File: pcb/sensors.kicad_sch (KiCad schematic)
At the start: 6 parts, among them U3 INA230AIRGTT, U4 MCP9804_DFN, U6 INA230AIRGTT, U7 INA230AIRGTT

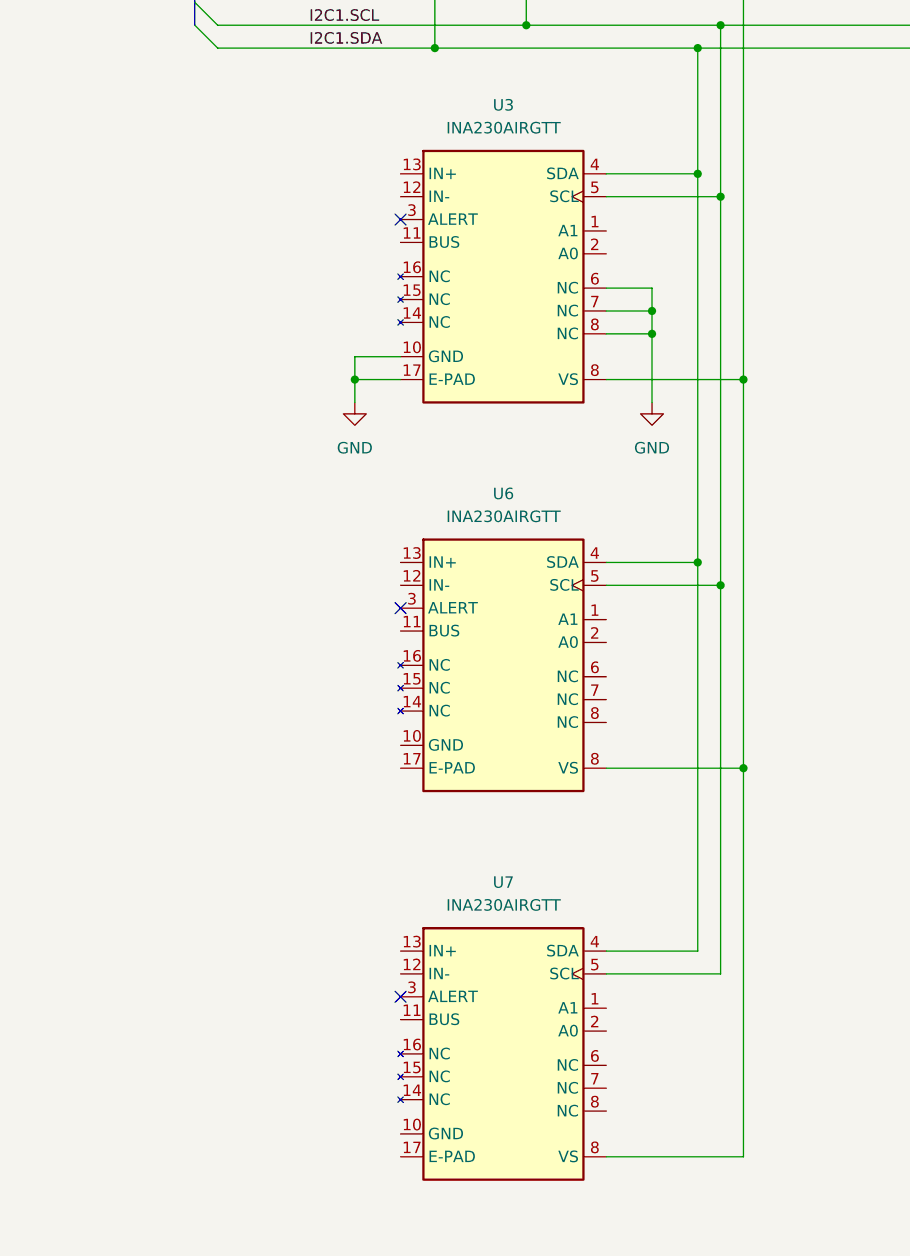
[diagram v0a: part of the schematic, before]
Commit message: hierarchical current sense
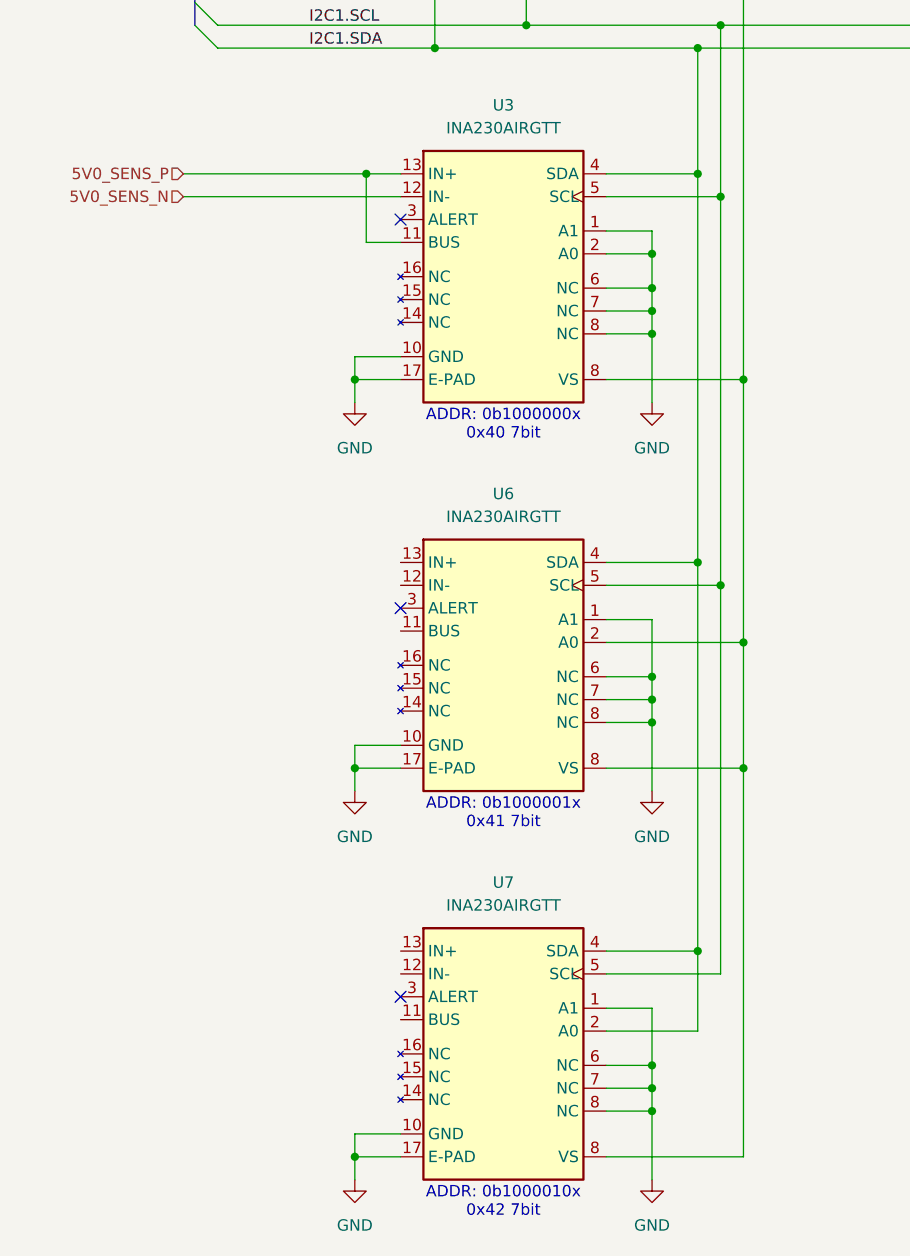
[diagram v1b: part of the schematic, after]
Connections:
- net 3V3: now also U6.2 (A0)
- net GND: now also U3.1 (A1), U3.2 (A0), U6.1 (A1), U6.10 (GND), U6.17 (E-PAD), U6.6 (NC), U6.7 (NC), U6.8 (VS), U7.1 (A1), U7.10 (GND), U7.17 (E-PAD), U7.6 (NC), U7.7 (NC), U7.8 (VS)
- net I2C1.SDA: now also U7.2 (A0)
- net 5V0_SENS_P: now reaches U3.11 (BUS)
- net 5V0_SENS_P: now also U3.13 (IN+)
- net 5V0_SENS_N: now reaches U3.12 (IN-)
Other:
- note added: "ADDR: 0b1000000x 0x40 7bit"
- note added: "ADDR: 0b1000001x 0x41 7bit"
- note added: "ADDR: 0b1000010x 0x42 7bit"

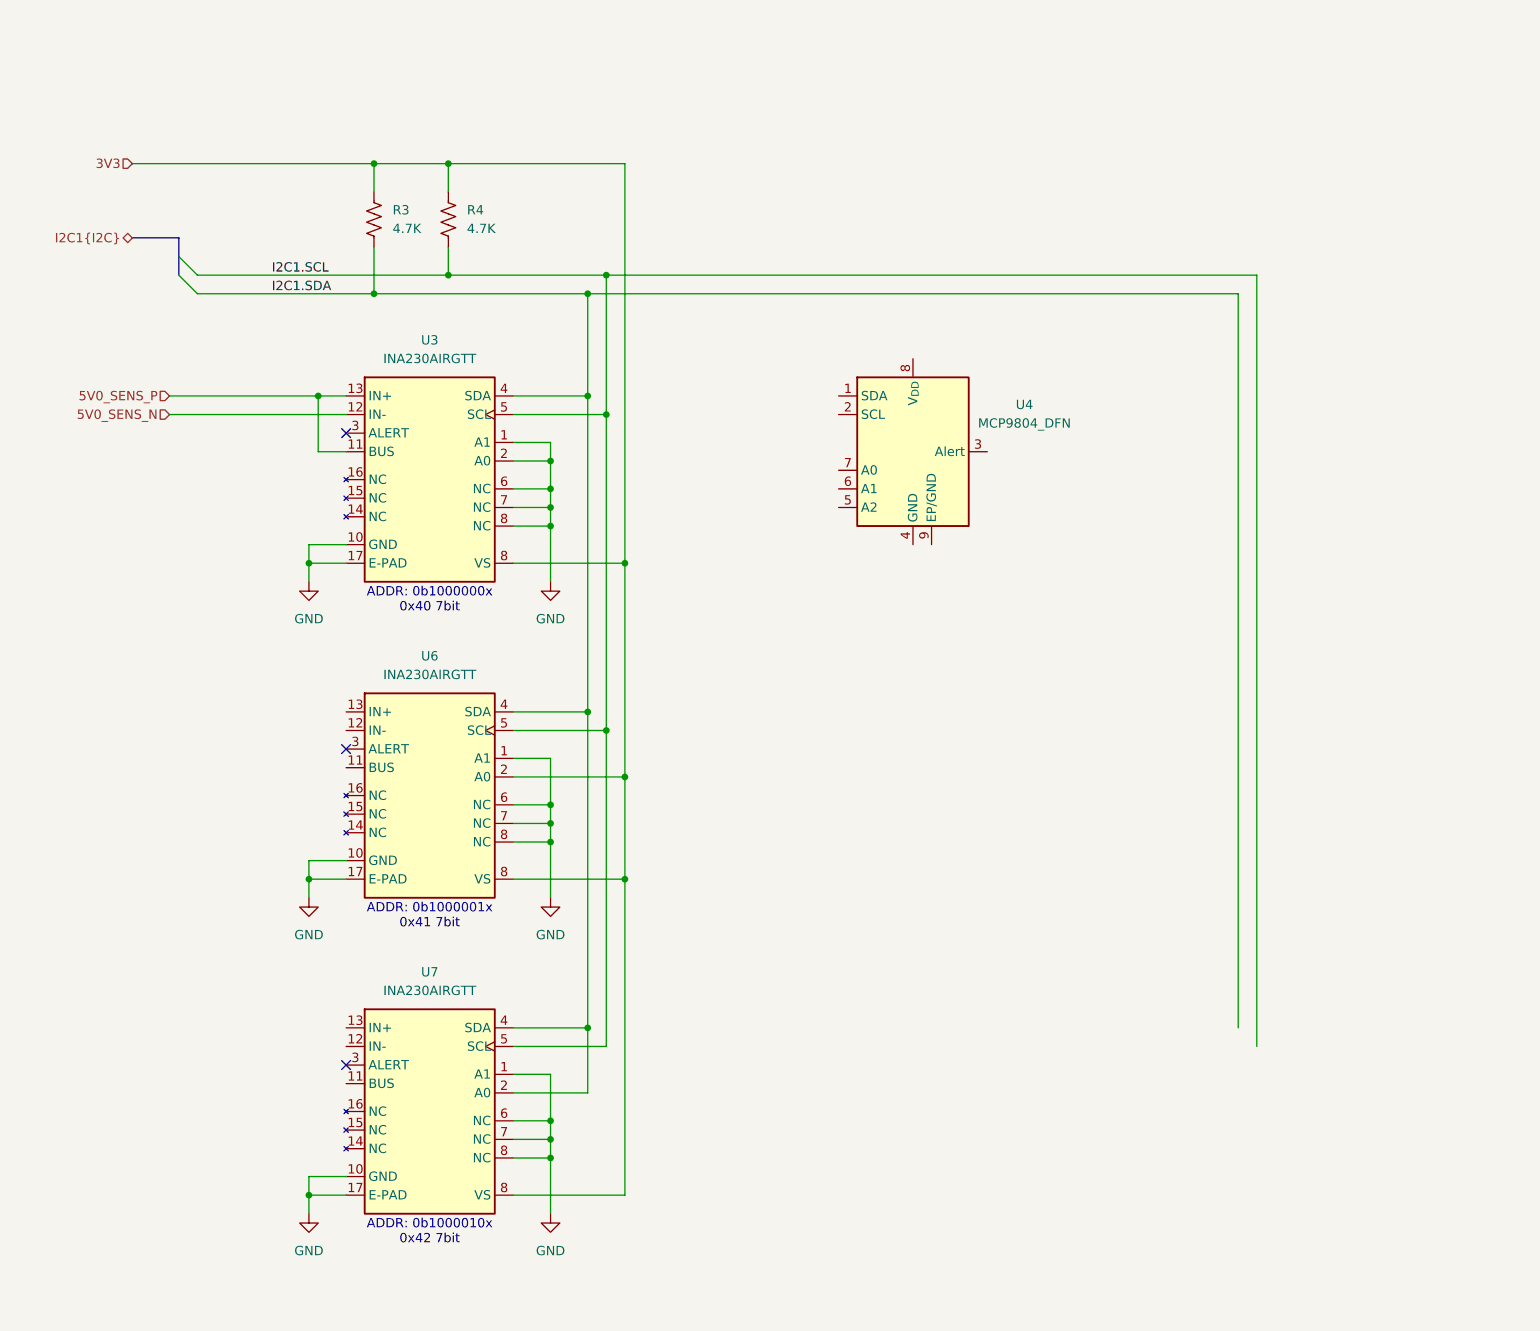
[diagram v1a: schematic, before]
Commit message: current sense hierarchy definition
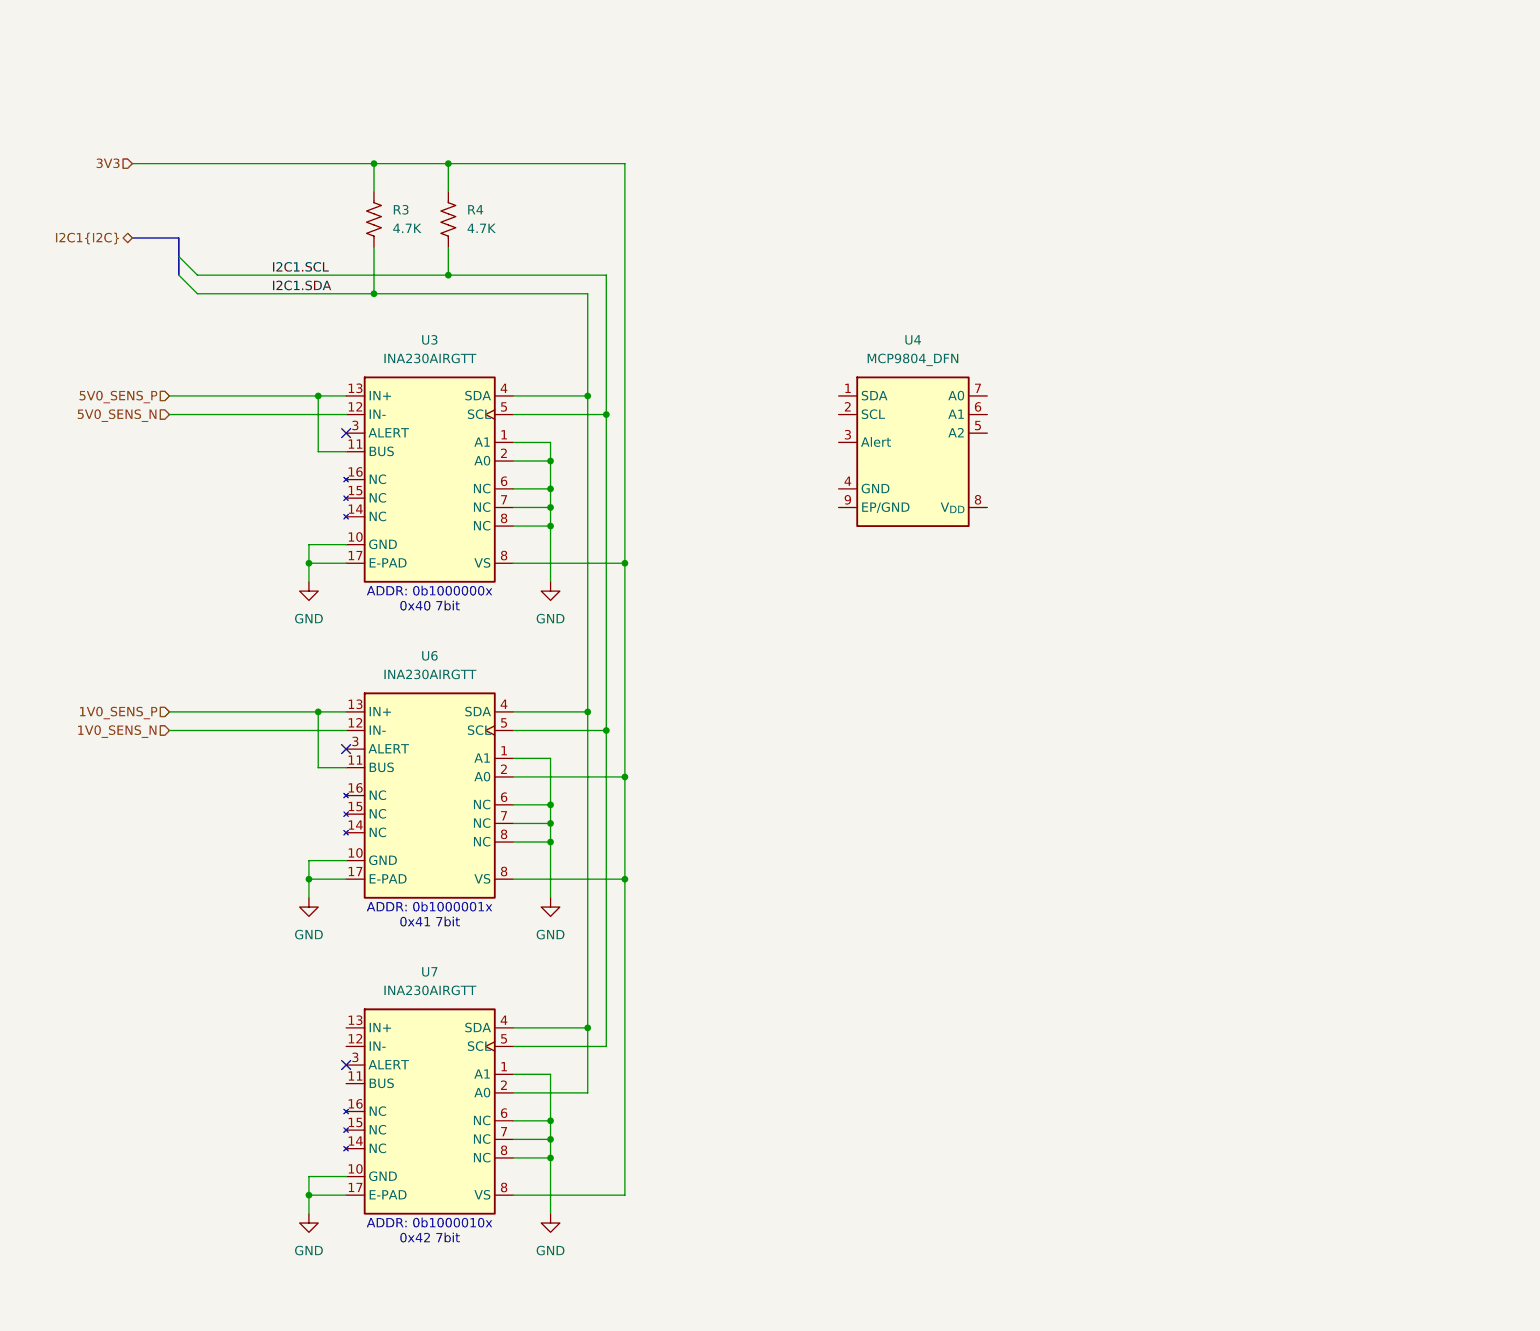
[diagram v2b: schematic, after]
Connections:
- net 1V0_SENS_P: now reaches U6.11 (BUS)
- net 1V0_SENS_P: now also U6.13 (IN+)
- net 1V0_SENS_N: now reaches U6.12 (IN-)
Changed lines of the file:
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@@
-	)
-	(junction
-		(at 104.14 54.61)
-		(diameter 0)
-		(color 0 0 0 0)
 	)
 	(junction
@@
 	)
 	(junction
+		(at 67.31 111.76)
+		(diameter 0)
+		(color 0 0 0 0)
+	)
+	(junction
 		(at 85.09 36.83)
 		(diameter 0)
@@
 	(junction
 		(at 106.68 71.12)
-		(diameter 0)
-		(color 0 0 0 0)
-	)
-	(junction
-		(at 106.68 52.07)
 		(diameter 0)
 		(color 0 0 0 0)
@@
 	(wire
 		(pts
+			(xy 46.99 114.3) (xy 71.12 114.3)
+		)
+		(stroke
+			(width 0)
+			(type default)
+		)
+	)
+	(wire
+		(pts
 			(xy 99.06 118.11) (xy 99.06 124.46)
 		)
@@
 	(wire
 		(pts
-			(xy 193.04 54.61) (xy 193.04 154.94)
-		)
-		(stroke
-			(width 0)
-			(type default)
-		)
-	)
-	(wire
-		(pts
 			(xy 104.14 154.94) (xy 104.14 111.76)
 		)
@@
 	(wire
 		(pts
+			(xy 46.99 111.76) (xy 67.31 111.76)
+		)
+		(stroke
+			(width 0)
+			(type default)
+		)
+	)
+	(wire
+		(pts
 			(xy 99.06 170.18) (xy 99.06 172.72)
 		)
@@
 	(wire
 		(pts
-			(xy 195.58 52.07) (xy 195.58 157.48)
-		)
-		(stroke
-			(width 0)
-			(type default)
-		)
-	)
-	(wire
-		(pts
 			(xy 109.22 91.44) (xy 93.98 91.44)
 		)
@@
 	(wire
 		(pts
-			(xy 195.58 52.07) (xy 106.68 52.07)
-		)
-		(stroke
-			(width 0)
-			(type default)
-		)
-	)
-	(wire
-		(pts
 			(xy 99.06 124.46) (xy 99.06 127)
 		)
@@
 	(wire
 		(pts
+			(xy 67.31 119.38) (xy 67.31 111.76)
+		)
+		(stroke
+			(width 0)
+			(type default)
+		)
+	)
+	(wire
+		(pts
 			(xy 93.98 127) (xy 99.06 127)
 		)
@@
 	(wire
 		(pts
+			(xy 67.31 111.76) (xy 71.12 111.76)
+		)
+		(stroke
+			(width 0)
+			(type default)
+		)
+	)
+	(wire
+		(pts
 			(xy 93.98 118.11) (xy 99.06 118.11)
 		)
@@
 	(wire
 		(pts
-			(xy 193.04 54.61) (xy 104.14 54.61)
-		)
-		(stroke
-			(width 0)
-			(type default)
-		)
-	)
-	(wire
-		(pts
 			(xy 99.06 129.54) (xy 99.06 137.16)
 		)
@@
 			(type default)
 			(color 0 0 255 1)
+		)
+	)
+	(wire
+		(pts
+			(xy 71.12 119.38) (xy 67.31 119.38)
+		)
+		(stroke
+			(width 0)
+			(type default)
 		)
 	)
@@
 		)
 	)
+	(hierarchical_label "1V0_SENS_P"
+		(shape input)
+		(at 46.99 111.76 180)
+		(effects
+			(font
+				(size 1.27 1.27)
+			)
+			(justify right)
+		)
+	)
 	(hierarchical_label "5V0_SENS_P"
 		(shape input)
 		(at 46.99 68.58 180)
+		(effects
+			(font
+				(size 1.27 1.27)
+			)
+			(justify right)
+		)
+	)
+	(hierarchical_label "1V0_SENS_N"
+		(shape input)
+		(at 46.99 114.3 180)
 		(effects
 			(font
@@
 		(fields_autoplaced yes)
 		(property "Reference" "U4"
-			(at 163.83 69.7798 0)
+			(at 148.59 60.96 0)
 			(effects
 				(font
@@
 		)
 		(property "Value" "MCP9804_DFN"
-			(at 163.83 72.3198 0)
+			(at 148.59 63.5 0)
 			(effects
 				(font
@@
 			(at 148.59 76.2 0)
 			(effects
+				(font
+					(size 1.27 1.27)
+				)
+				(hide yes)
+			)
+		)
+		(property "Name" ""
+			(at 148.59 76.2 0)
+			(effects

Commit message: removed one I-sense
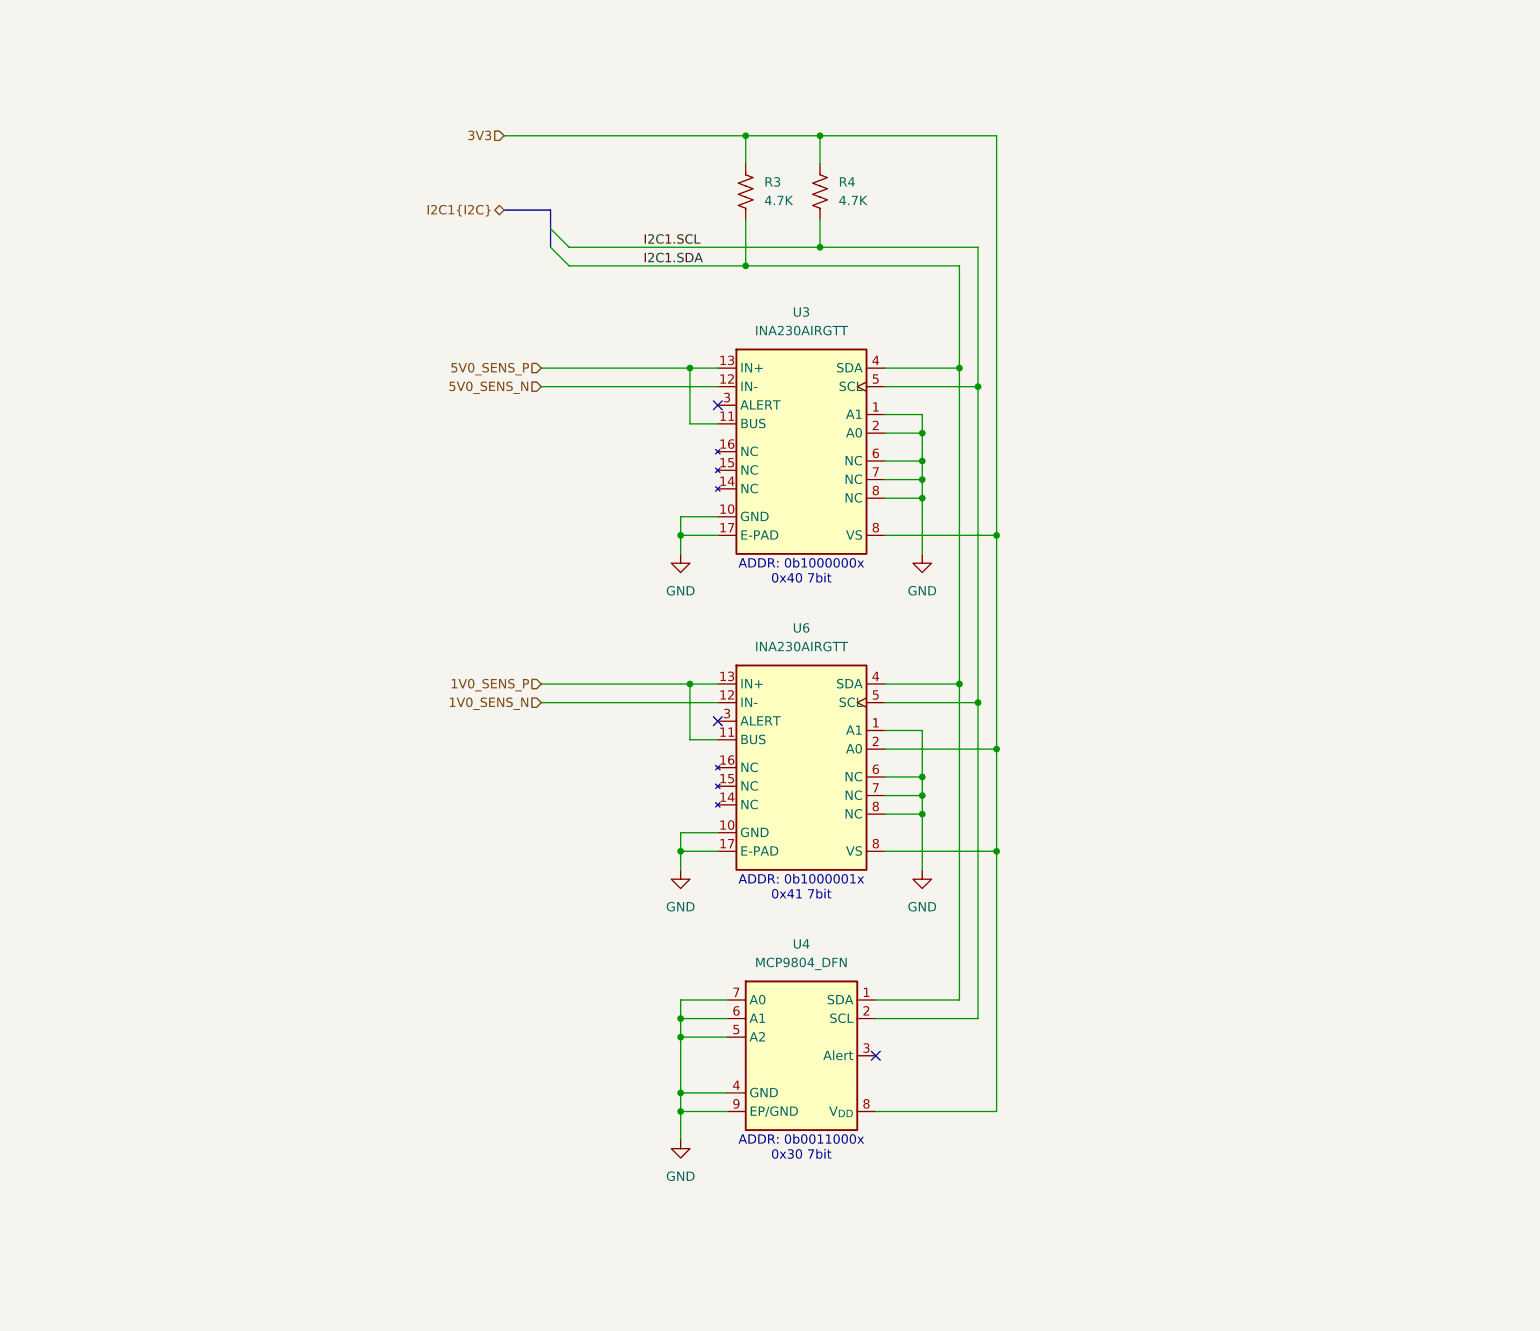
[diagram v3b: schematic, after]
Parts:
- removed U7: INA230AIRGTT, Package_DFN_QFN:VQFN-16-1EP_3x3mm_P0.5mm_EP1.6x1.6mm, symbol Sensor_Current:INA230AIRGTT
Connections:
- net 3V3: now also U4.8 (V_{DD})
- net GND: now also U4.4 (GND), U4.5 (A2), U4.6 (A1), U4.7 (A0), U4.9 (EP/GND)
- net I2C1.SCL: now also U4.2 (SCL)
- net I2C1.SDA: now also U4.1 (SDA)
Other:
- note added: "ADDR: 0b0011000x 0x30 7bit"
- note removed: "ADDR: 0b1000010x 0x42 7bit"
- moved on the sheet: R3, R4, U3, U4, U6

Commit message: saved libraries to project
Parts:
- R3, R4: symbol Device:R_US -> library:R_US
- U3: symbol Sensor_Current:INA230AIRGTT -> library:INA230AIRGTT_1
- U4: symbol Sensor_Temperature:MCP9804_DFN -> library:MCP9804_DFN
- U6: symbol Sensor_Current:INA230AIRGTT -> library:INA230AIRGTT_2
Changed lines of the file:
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@@
 	)
 	(symbol
-		(lib_id "power:GND")
+		(lib_id "library:GND")
 		(at 149.86 133.35 0)
 		(unit 1)
@@
 	)
 	(symbol
-		(lib_id "Device:R_US")
+		(lib_id "library:R_US")
 		(at 125.73 40.64 0)
 		(unit 1)
@@
 	)
 	(symbol
-		(lib_id "Sensor_Temperature:MCP9804_DFN")
+		(lib_id "library:MCP9804_DFN")
 		(at 133.35 158.75 0)
 		(unit 1)
@@
 	)
 	(symbol
-		(lib_id "power:GND")
+		(lib_id "library:GND")
 		(at 149.86 90.17 0)
 		(unit 1)
@@
 	)
 	(symbol
-		(lib_id "power:GND")
+		(lib_id "library:GND")
 		(at 116.84 170.18 0)
 		(unit 1)
@@
 	)
 	(symbol
-		(lib_id "power:GND")
+		(lib_id "library:GND")
 		(at 116.84 90.17 0)
 		(unit 1)
@@
 	)
 	(symbol
-		(lib_name "INA230AIRGTT_1")
-		(lib_id "Sensor_Current:INA230AIRGTT")
+		(lib_name "INA230AIRGTT_1_1")
+		(lib_id "library:INA230AIRGTT_1")
 		(at 133.35 76.2 0)
 		(unit 1)
@@
 	)
 	(symbol
-		(lib_id "power:GND")
+		(lib_id "library:GND")
 		(at 116.84 133.35 0)
 		(unit 1)
@@
 	)
 	(symbol
-		(lib_id "Device:R_US")
+		(lib_id "library:R_US")
 		(at 135.89 40.64 0)
 		(unit 1)
@@
 	)
 	(symbol
-		(lib_name "INA230AIRGTT_2")
-		(lib_id "Sensor_Current:INA230AIRGTT")
+		(lib_name "INA230AIRGTT_2_1")
+		(lib_id "library:INA230AIRGTT_2")
 		(at 133.35 119.38 0)
 		(unit 1)
